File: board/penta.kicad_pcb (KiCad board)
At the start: 2 copper layers, 37.4 x 37.4 mm, 137 parts, among them J1 USB_C_Receptacle_PowerOnly_6P, U1 XIAO-RP2040-SMD

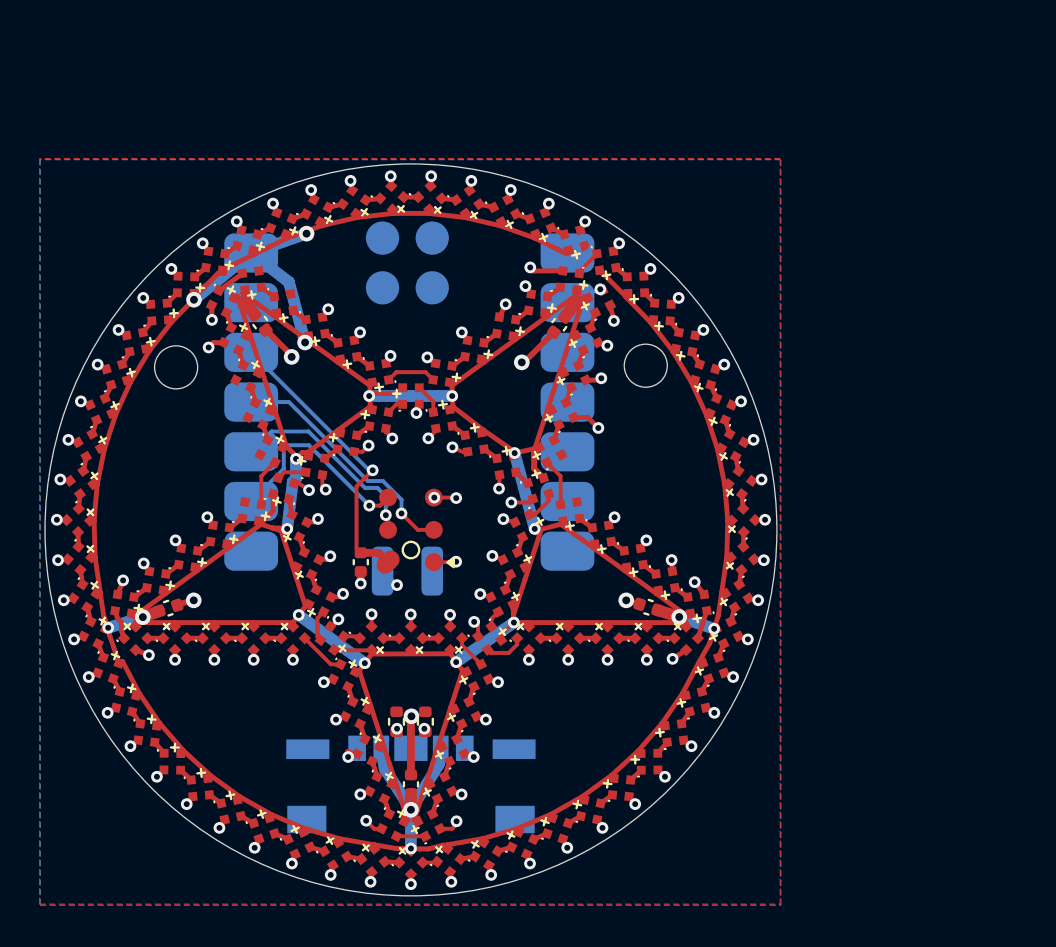
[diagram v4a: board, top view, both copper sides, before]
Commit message: myriad improvements. mounting points for idk, nice symmetric. removed unnecessary pads from seeduino footprint to make room for mount points; added exposed ldo VIN pin to seeduino footprint bc it's VBUS >| VIN so it can supply leds (and made those pins longer so they can be manually soldered and still; improved zone fills;
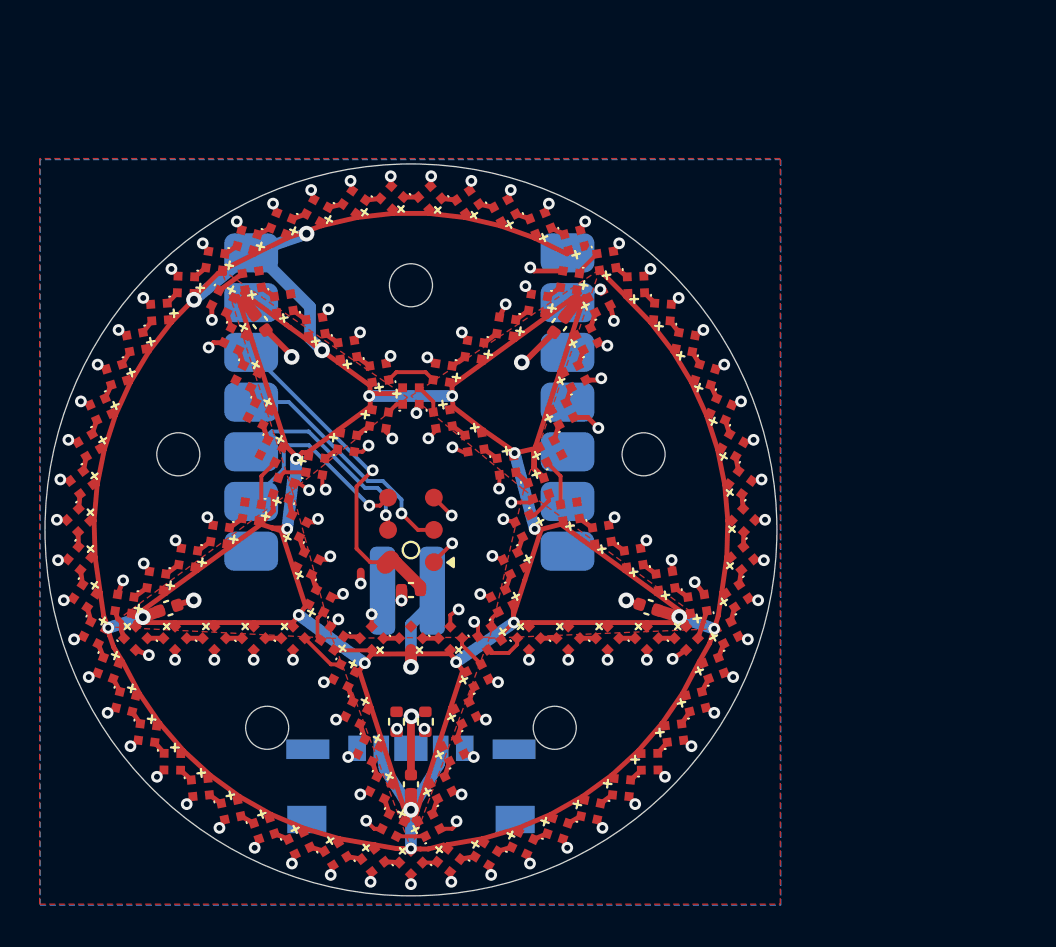
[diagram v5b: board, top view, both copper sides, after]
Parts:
- moved C1 2.93 mm to (100.0, 103.1), turned to 180 degrees
- moved G*** 0.60 mm to (100.0, 107.6)
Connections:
- U1 pad 15: unconnected-(U1-BAT-Pad15) -> +5V
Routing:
- net +5V: track 297.5 -> 305.4 mm, vias 19 -> 20
- net +3V3: track 14.9 -> 17.3 mm
- net GND: track 82.3 -> 81.7 mm, vias 127 -> 125
- added copper zone on F.Cu, net +5V
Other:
- outline, holes or cut-outs redrawn

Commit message: add 3 gpios to the screwmounts, which are now thts. maybe these can be used for capacitive touch?
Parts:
- added TP1: TestPoint, penta:ScrewTouchHole, F.Cu at (100.0, 87.5)
- added TP2: TestPoint, penta:ScrewTouchHole, F.Cu at (111.9, 96.1)
- added TP3: TestPoint, penta:ScrewTouchHole, F.Cu at (107.3, 110.1)
- added TP4: TestPoint, penta:ScrewTouchHole, F.Cu at (92.7, 110.1)
- added TP5: TestPoint, penta:ScrewTouchHole, F.Cu at (88.1, 96.1)
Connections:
- U1 pad 1: unconnected-(U1-GPIO26_A0_D0-Pad1) -> /TOUCH1
- U1 pad 5: unconnected-(U1-GPIO6_D4_SDA-Pad5) -> /TOUCH2
- U1 pad 8: unconnected-(U1-GPIO1_D7_CSn_RX-Pad8) -> /TOUCH3
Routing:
- net /TOUCH1: track 0.00 -> 8.68 mm
- net Net-(J1-SHIELD): track 0.00 -> 7.22 mm
- net /TOUCH3: track 0.00 -> 6.49 mm
- net /TOUCH2: track 0.00 -> 3.94 mm
- net +5V: track 305.4 -> 306.9 mm
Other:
- outline, holes or cut-outs redrawn

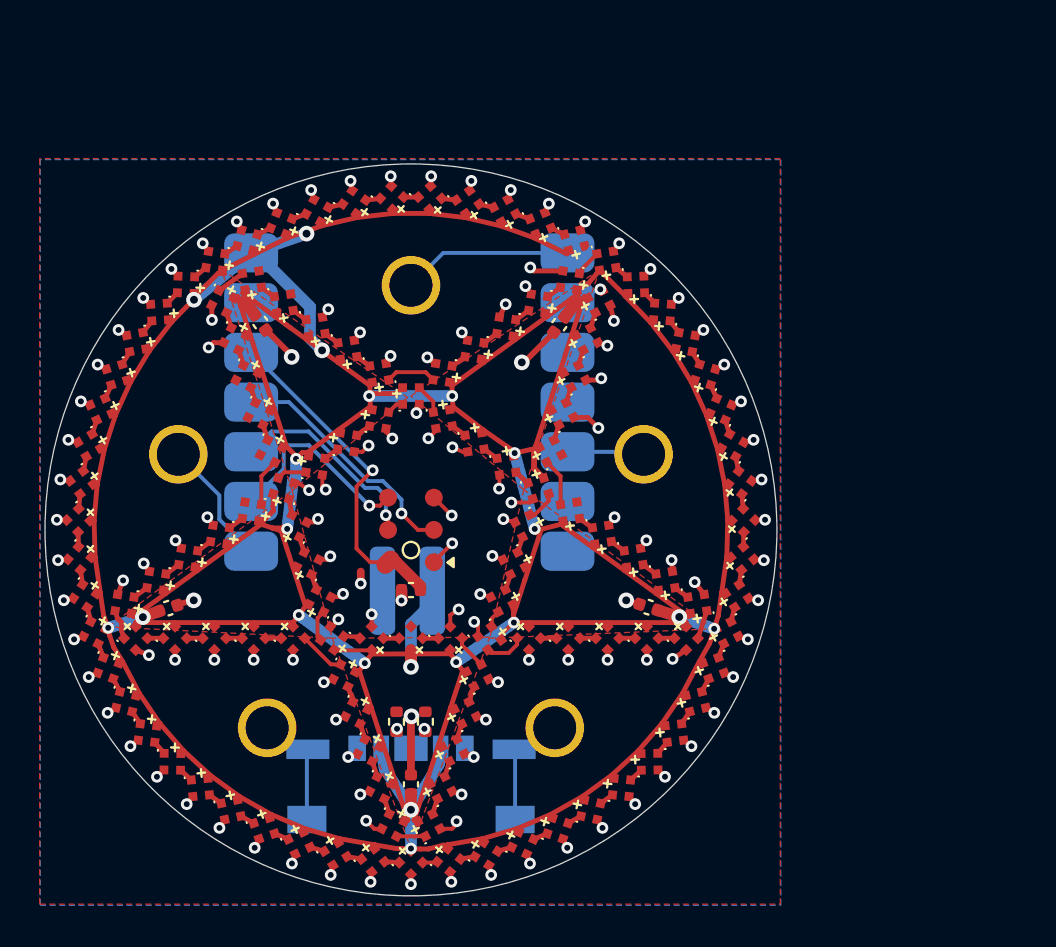
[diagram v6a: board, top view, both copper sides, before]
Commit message: add an nfet so we can power down pixels for whatever saves that'll get doing larger pattern work; make 4-layer board to support switching a gnd plane off; decorate
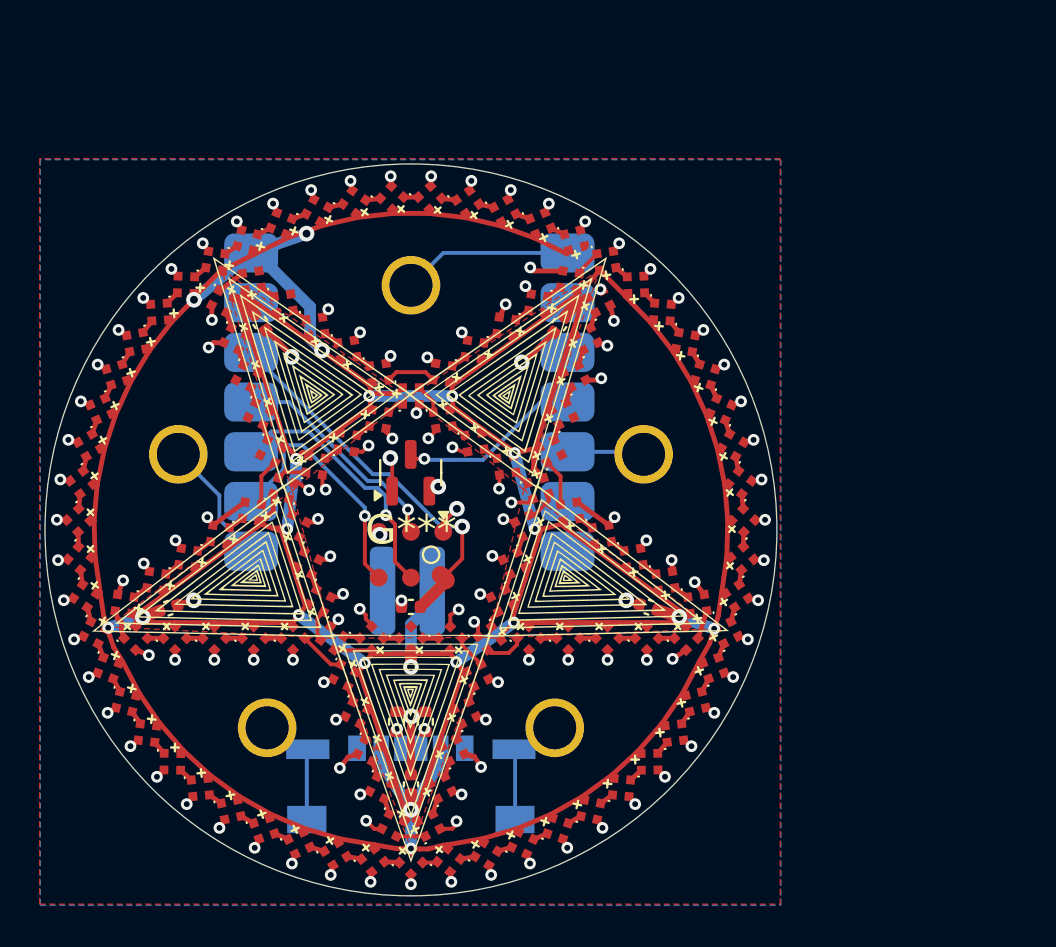
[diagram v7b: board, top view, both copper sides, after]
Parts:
- added G***: LOGO, LOGO, F.Cu at (100.0, 100.0)
- added Q1: SK335N, Package_TO_SOT_SMD:SOT-23, F.Cu at (100.0, 97.1)
- moved MIC1 1.27 mm to (100.0, 101.3), turned to 180 degrees
- moved C1 0.86 mm to (100.0, 103.9)
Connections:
- D1 pad 3: GND -> /PXL_GND
- D10 pad 3: GND -> /PXL_GND
- D100 pad 3: GND -> /PXL_GND
- D101 pad 3: GND -> /PXL_GND
- D102 pad 3: GND -> /PXL_GND
- D103 pad 3: GND -> /PXL_GND
- D104 pad 3: GND -> /PXL_GND
- D105 pad 3: GND -> /PXL_GND
- D106 pad 3: GND -> /PXL_GND
- D107 pad 3: GND -> /PXL_GND
- D108 pad 3: GND -> /PXL_GND
- D109 pad 3: GND -> /PXL_GND
- D11 pad 3: GND -> /PXL_GND
- D110 pad 3: GND -> /PXL_GND
- D111 pad 3: GND -> /PXL_GND
- D112 pad 3: GND -> /PXL_GND
- D113 pad 3: GND -> /PXL_GND
- D114 pad 3: GND -> /PXL_GND
- D115 pad 3: GND -> /PXL_GND
- D116 pad 3: GND -> /PXL_GND
- D117 pad 3: GND -> /PXL_GND
- D118 pad 3: GND -> /PXL_GND
- D119 pad 3: GND -> /PXL_GND
- D12 pad 3: GND -> /PXL_GND
- D120 pad 3: GND -> /PXL_GND
- D121 pad 3: GND -> /PXL_GND
- D122 pad 3: GND -> /PXL_GND
- D123 pad 3: GND -> /PXL_GND
- D124 pad 3: GND -> /PXL_GND
- D125 pad 3: GND -> /PXL_GND
- D13 pad 3: GND -> /PXL_GND
- D14 pad 3: GND -> /PXL_GND
- D15 pad 3: GND -> /PXL_GND
- D16 pad 3: GND -> /PXL_GND
- D17 pad 3: GND -> /PXL_GND
- D18 pad 3: GND -> /PXL_GND
- D19 pad 3: GND -> /PXL_GND
- D2 pad 3: GND -> /PXL_GND
- D20 pad 3: GND -> /PXL_GND
- D21 pad 3: GND -> /PXL_GND
- D22 pad 3: GND -> /PXL_GND
- D23 pad 3: GND -> /PXL_GND
- D24 pad 3: GND -> /PXL_GND
- D25 pad 3: GND -> /PXL_GND
- D26 pad 3: GND -> /PXL_GND
- D27 pad 3: GND -> /PXL_GND
- D28 pad 3: GND -> /PXL_GND
- D29 pad 3: GND -> /PXL_GND
- D3 pad 3: GND -> /PXL_GND
- D30 pad 3: GND -> /PXL_GND
- D31 pad 3: GND -> /PXL_GND
- D32 pad 3: GND -> /PXL_GND
- D33 pad 3: GND -> /PXL_GND
- D34 pad 3: GND -> /PXL_GND
- D35 pad 3: GND -> /PXL_GND
- D36 pad 3: GND -> /PXL_GND
- D37 pad 3: GND -> /PXL_GND
- D38 pad 3: GND -> /PXL_GND
- D39 pad 3: GND -> /PXL_GND
- D4 pad 3: GND -> /PXL_GND
- D40 pad 3: GND -> /PXL_GND
- D41 pad 3: GND -> /PXL_GND
- D42 pad 3: GND -> /PXL_GND
- D43 pad 3: GND -> /PXL_GND
- D44 pad 3: GND -> /PXL_GND
- D45 pad 3: GND -> /PXL_GND
- D46 pad 3: GND -> /PXL_GND
- D47 pad 3: GND -> /PXL_GND
- D48 pad 3: GND -> /PXL_GND
- D49 pad 3: GND -> /PXL_GND
- D5 pad 3: GND -> /PXL_GND
- D50 pad 3: GND -> /PXL_GND
- D51 pad 3: GND -> /PXL_GND
- D52 pad 3: GND -> /PXL_GND
- D53 pad 3: GND -> /PXL_GND
- D54 pad 3: GND -> /PXL_GND
- D55 pad 3: GND -> /PXL_GND
- D56 pad 3: GND -> /PXL_GND
- D57 pad 3: GND -> /PXL_GND
- D58 pad 3: GND -> /PXL_GND
- D59 pad 3: GND -> /PXL_GND
- D6 pad 3: GND -> /PXL_GND
- D60 pad 3: GND -> /PXL_GND
- D61 pad 3: GND -> /PXL_GND
- D62 pad 3: GND -> /PXL_GND
- D63 pad 3: GND -> /PXL_GND
- D64 pad 3: GND -> /PXL_GND
- D65 pad 3: GND -> /PXL_GND
- D66 pad 3: GND -> /PXL_GND
- D67 pad 3: GND -> /PXL_GND
- D68 pad 3: GND -> /PXL_GND
- D69 pad 3: GND -> /PXL_GND
- D7 pad 3: GND -> /PXL_GND
- D70 pad 3: GND -> /PXL_GND
- D71 pad 3: GND -> /PXL_GND
- D72 pad 3: GND -> /PXL_GND
- D73 pad 3: GND -> /PXL_GND
- D74 pad 3: GND -> /PXL_GND
- D75 pad 3: GND -> /PXL_GND
- D76 pad 3: GND -> /PXL_GND
- D77 pad 3: GND -> /PXL_GND
- D78 pad 3: GND -> /PXL_GND
- D79 pad 3: GND -> /PXL_GND
- D8 pad 3: GND -> /PXL_GND
- D80 pad 3: GND -> /PXL_GND
- D81 pad 3: GND -> /PXL_GND
- D82 pad 3: GND -> /PXL_GND
- D83 pad 3: GND -> /PXL_GND
- D84 pad 3: GND -> /PXL_GND
- D85 pad 3: GND -> /PXL_GND
- D86 pad 3: GND -> /PXL_GND
- D87 pad 3: GND -> /PXL_GND
- D88 pad 3: GND -> /PXL_GND
- D89 pad 3: GND -> /PXL_GND
- D9 pad 3: GND -> /PXL_GND
- D90 pad 3: GND -> /PXL_GND
- D91 pad 3: GND -> /PXL_GND
- D92 pad 3: GND -> /PXL_GND
- D93 pad 3: GND -> /PXL_GND
- D94 pad 3: GND -> /PXL_GND
- D95 pad 3: GND -> /PXL_GND
- D96 pad 3: GND -> /PXL_GND
- D97 pad 3: GND -> /PXL_GND
- D98 pad 3: GND -> /PXL_GND
- D99 pad 3: GND -> /PXL_GND
- U1 pad 4: unconnected-(U1-GPIO29_A3_D3-Pad4) -> /EN_PIXELS
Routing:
- net /PXL_GND: track 0.00 -> 75.2 mm, vias 0 -> 116
- net GND: track 81.7 -> 12.7 mm, vias 125 -> 9
- net /EN_PIXELS: track 0.00 -> 9.35 mm, vias 0 -> 1
- net /I2S DATA: track 10.4 -> 13.4 mm
- net /BCLK: track 10.2 -> 12.8 mm
- net +3V3: track 17.3 -> 19.5 mm
- net /LRCLK: track 12.5 -> 11.5 mm
- added copper zone on F.Cu, net /PXL_GND
- added copper zone on In1.Cu, net /PXL_GND
- added copper zone on In2.Cu, net GND
- removed copper zone on F.Cu, net GND
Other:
- copper layers 2 -> 4

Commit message: pins rearrangement to make touch pads work; minor fixes and polish
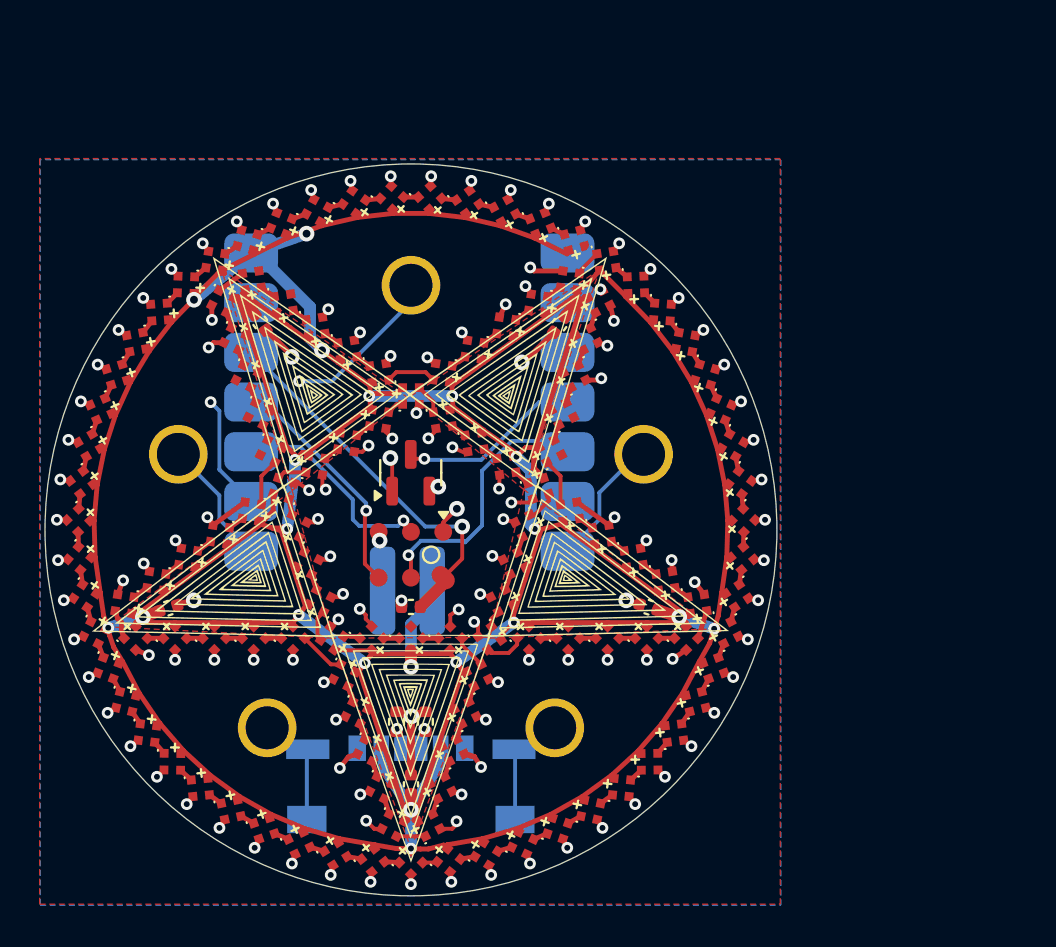
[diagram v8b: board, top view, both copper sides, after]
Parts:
- TP0: renamed from TP2; value TestPoint -> TouchPoint
- TP1: renamed from TP5; value TestPoint -> TouchPoint
- TP2: renamed from TP1; value TestPoint -> TouchPoint
- TP3, TP4: value TestPoint -> TouchPoint
- turned D101 to -7.363 degrees
- turned D103 to -20.454 degrees
- turned D110 to -66.272 degrees
- turned D112 to -79.363 degrees
- turned D114 to -92.454 degrees
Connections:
- TP0 pad 1: /TOUCH2 -> /TOUCH0
- TP1 pad 1: /TOUCH3 -> /TOUCH1
- TP2 pad 1: /TOUCH1 -> /TOUCH2
- U1 pad 1: /TOUCH1 -> unconnected-(U1-GPIO26_A0_D0-Pad1)
- U1 pad 10: /I2S DATA -> /LRCLK
- U1 pad 11: /LRCLK -> /BCLK
- U1 pad 5: /TOUCH2 -> /I2S DATA
- U1 pad 7: unconnected-(U1-GPIO0_D6_TX-Pad7) -> /TOUCH0
- U1 pad 8: /TOUCH3 -> /TOUCH1
- U1 pad 9: /BCLK -> /TOUCH2
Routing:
- net /TOUCH2: track 3.94 -> 19.2 mm, vias 0 -> 2
- net /TOUCH3: track 6.49 -> 0.00 mm
- net /TOUCH0: track 0.00 -> 6.39 mm
- net /TOUCH1: track 8.68 -> 6.49 mm
- net /BCLK: track 12.8 -> 12.1 mm
- net /LRCLK: track 11.5 -> 11.0 mm
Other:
- board text added: "EN_LED"
- board text added: "T0"
- board text added: "T1"
- board text added: "T2"
